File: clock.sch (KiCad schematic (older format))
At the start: 20 parts, among them SW1 SW_Push, SW2 SW_SPDT, U23 LM555xN, U24 74LS04, U25 74LS08, U26 74LS32, U27 LM555xN, U28 LM555xN

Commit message: Let there be light
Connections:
- no-connect marks 3 -> 2
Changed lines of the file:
@@
 $Descr A4 11693 8268
 encoding utf-8
-Sheet 5 11
+Sheet 8 20
 Title ""
 Date ""
@@
 	1    0    0    -1
 $EndComp
-NoConn ~ 5450 5050
 $EndSCHEMATC

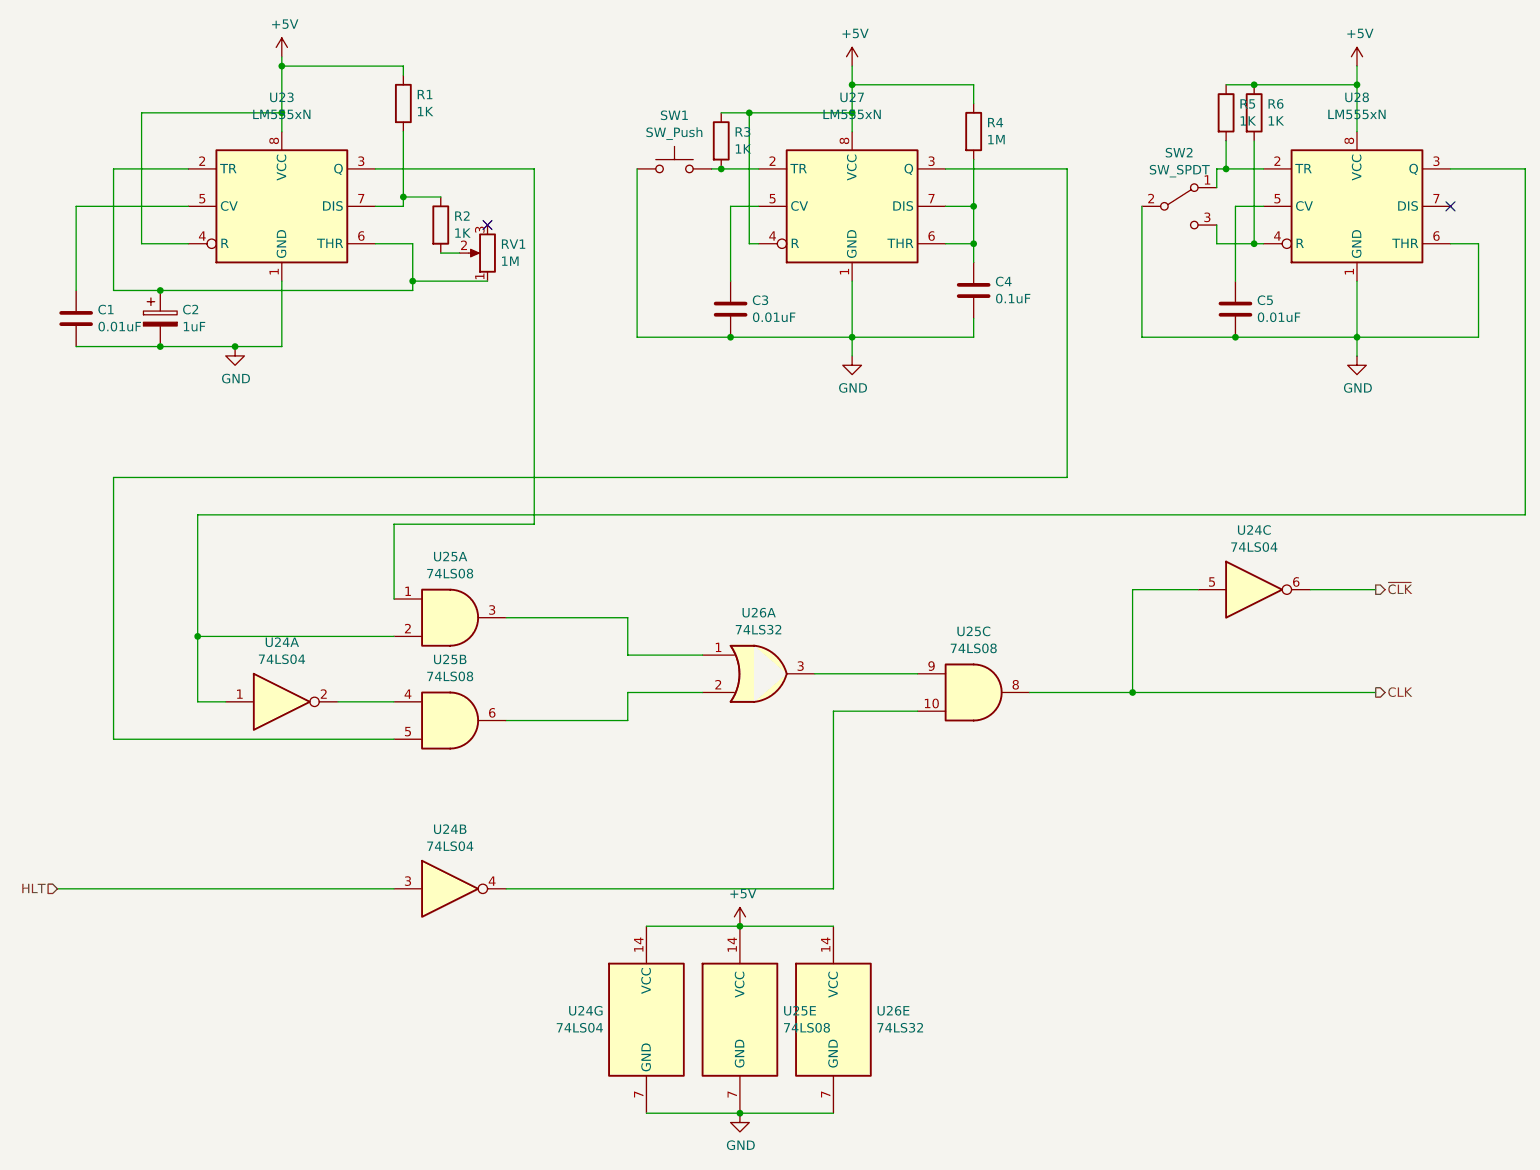
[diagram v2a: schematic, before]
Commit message: Added NAND GATES in ALU
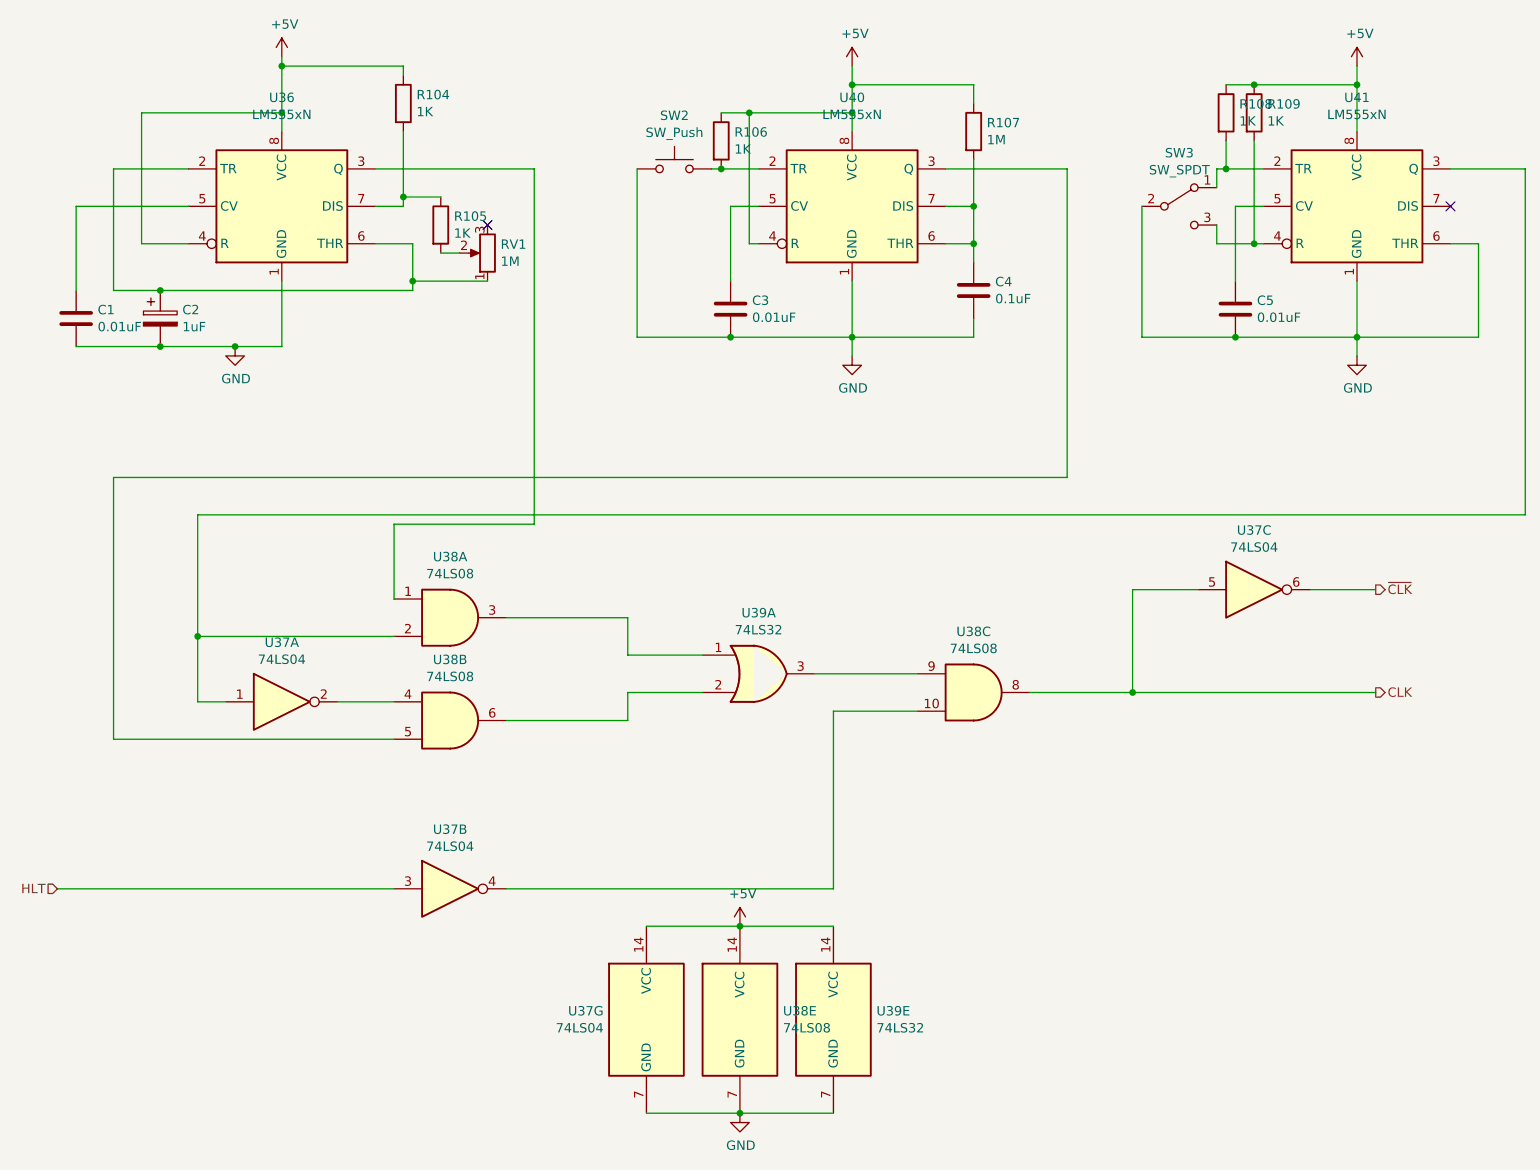
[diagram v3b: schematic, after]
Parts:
- renumbered R1 to R104, R2 to R105, R3 to R106, R4 to R107, R5 to R108, R6 to R109, SW1 to SW2, SW2 to SW3, U23 to U36, U24 to U37, U25 to U38, U26 to U39, U27 to U40, U28 to U41

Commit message: using new RAM and ROM,15bits baby
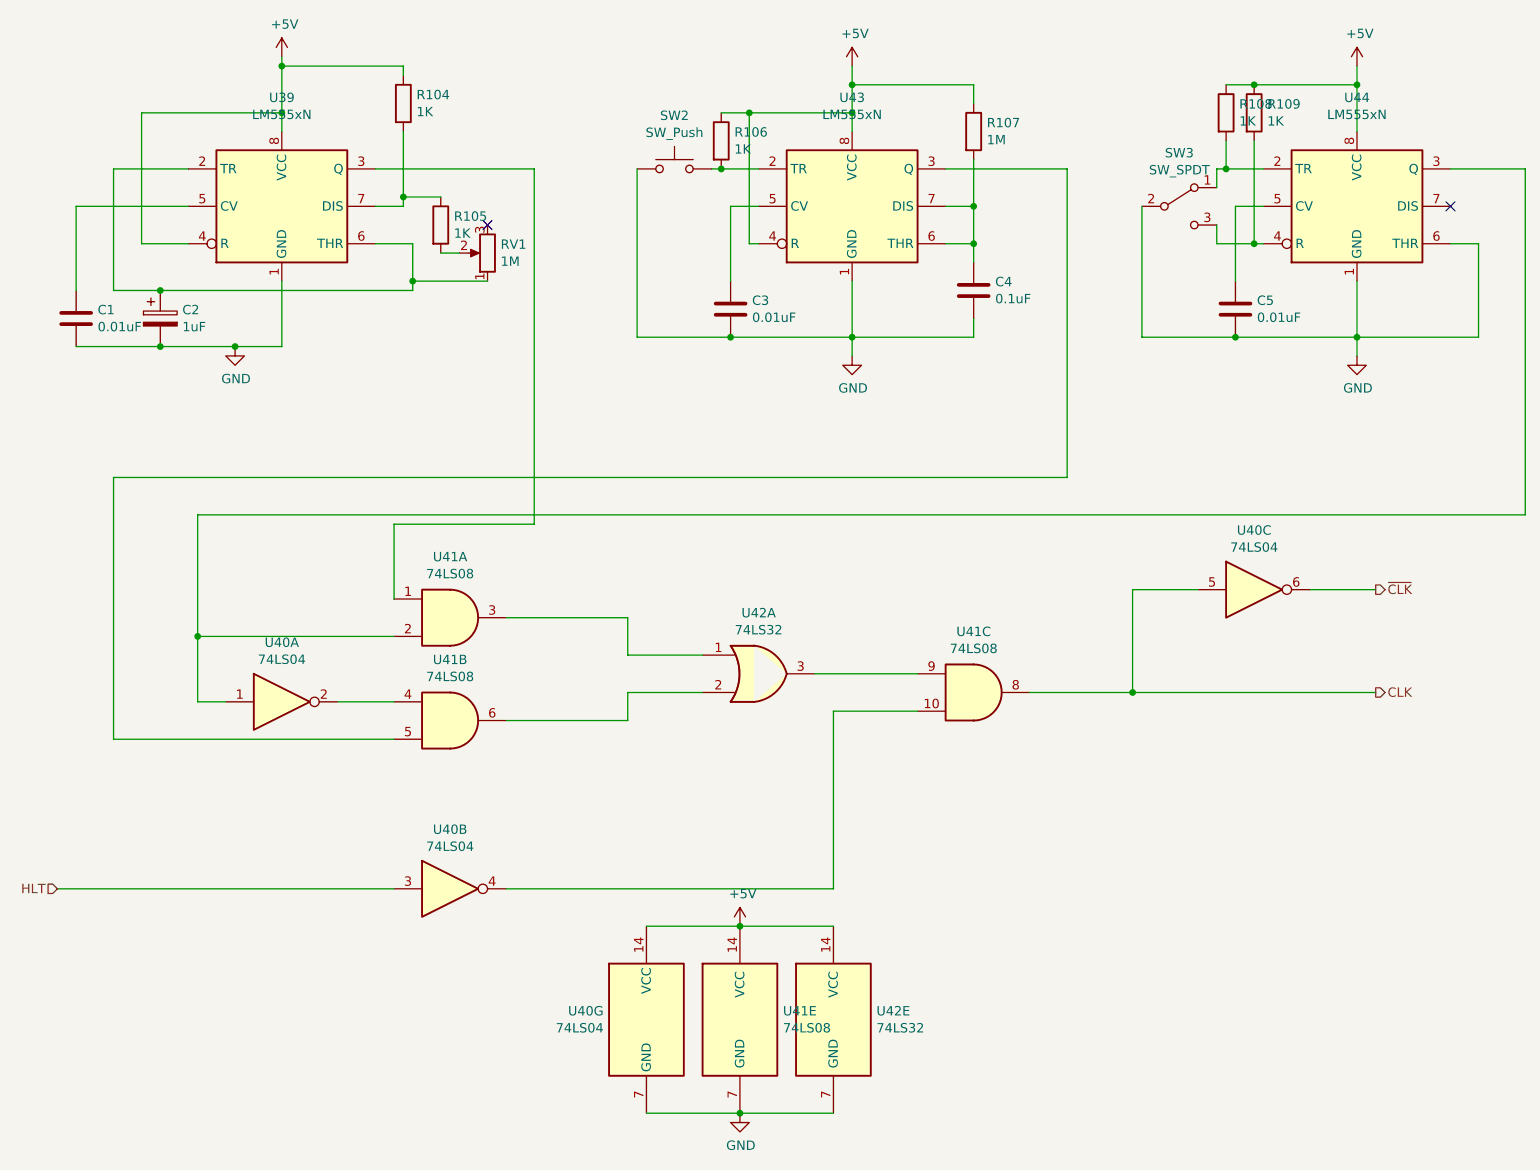
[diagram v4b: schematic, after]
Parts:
- renumbered U36 to U39, U37 to U40, U38 to U41, U39 to U42, U40 to U43, U41 to U44
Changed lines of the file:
@@
 P 2700 1100
 AR Path="/5F76260D" Ref="#PWR?"  Part="1"
-AR Path="/5F75E433/5F76260D" Ref="#PWR0151"  Part="1"
-F 0 "#PWR0151" H 2700 950 50  0001 C CNN
+AR Path="/5F75E433/5F76260D" Ref="#PWR0156"  Part="1"
+F 0 "#PWR0156" H 2700 950 50  0001 C CNN
 F 1 "+5V" H 2715 1273 50  0000 C CNN
 F 2 "" H 2700 1100 50  0001 C CNN
@@
 P 5750 2700
 AR Path="/5F763381" Ref="#PWR?"  Part="1"
-AR Path="/5F75E433/5F763381" Ref="#PWR0155"  Part="1"
-F 0 "#PWR0155" H 5750 2450 50  0001 C CNN
+AR Path="/5F75E433/5F763381" Ref="#PWR0160"  Part="1"
+F 0 "#PWR0160" H 5750 2450 50  0001 C CNN
 F 1 "GND" H 5755 2527 50  0000 C CNN
 F 2 "" H 5750 2700 50  0001 C CNN
@@
 P 2450 2650
 AR Path="/5F7634B3" Ref="#PWR?"  Part="1"
-AR Path="/5F75E433/5F7634B3" Ref="#PWR0150"  Part="1"
-F 0 "#PWR0150" H 2450 2400 50  0001 C CNN
+AR Path="/5F75E433/5F7634B3" Ref="#PWR0155"  Part="1"
+F 0 "#PWR0155" H 2450 2400 50  0001 C CNN
 F 1 "GND" H 2455 2477 50  0000 C CNN
 F 2 "" H 2450 2650 50  0001 C CNN
@@
 P 5750 1150
 AR Path="/5F76F8D8" Ref="#PWR?"  Part="1"
-AR Path="/5F75E433/5F76F8D8" Ref="#PWR0154"  Part="1"
-F 0 "#PWR0154" H 5750 1000 50  0001 C CNN
+AR Path="/5F75E433/5F76F8D8" Ref="#PWR0159"  Part="1"
+F 0 "#PWR0159" H 5750 1000 50  0001 C CNN
 F 1 "+5V" H 5765 1323 50  0000 C CNN
 F 2 "" H 5750 1150 50  0001 C CNN
@@
 P 8450 2700
 AR Path="/5F785279" Ref="#PWR?"  Part="1"
-AR Path="/5F75E433/5F785279" Ref="#PWR0157"  Part="1"
-F 0 "#PWR0157" H 8450 2450 50  0001 C CNN
+AR Path="/5F75E433/5F785279" Ref="#PWR0162"  Part="1"
+F 0 "#PWR0162" H 8450 2450 50  0001 C CNN
 F 1 "GND" H 8455 2527 50  0000 C CNN
 F 2 "" H 8450 2700 50  0001 C CNN
@@
 P 8450 1150
 AR Path="/5F78527F" Ref="#PWR?"  Part="1"
-AR Path="/5F75E433/5F78527F" Ref="#PWR0156"  Part="1"
-F 0 "#PWR0156" H 8450 1000 50  0001 C CNN
+AR Path="/5F75E433/5F78527F" Ref="#PWR0161"  Part="1"
+F 0 "#PWR0161" H 8450 1000 50  0001 C CNN
 F 1 "+5V" H 8465 1323 50  0000 C CNN
 F 2 "" H 8450 1150 50  0001 C CNN
@@
 P 3600 4100
 AR Path="/5F7BE3EA" Ref="U?"  Part="1"
-AR Path="/5F75E433/5F7BE3EA" Ref="U38"  Part="1"
-F 0 "U38" H 3600 4425 50  0000 C CNN
+AR Path="/5F75E433/5F7BE3EA" Ref="U41"  Part="1"
+F 0 "U41" H 3600 4425 50  0000 C CNN
 F 1 "74LS08" H 3600 4334 50  0000 C CNN
 F 2 "Package_DIP:DIP-14_W7.62mm" H 3600 4100 50  0001 C CNN
@@
 P 3600 4650
 AR Path="/5F7C112B" Ref="U?"  Part="2"
-AR Path="/5F75E433/5F7C112B" Ref="U38"  Part="2"
-F 0 "U38" H 3600 4975 50  0000 C CNN
+AR Path="/5F75E433/5F7C112B" Ref="U41"  Part="2"
+F 0 "U41" H 3600 4975 50  0000 C CNN
 F 1 "74LS08" H 3600 4884 50  0000 C CNN
 F 2 "Package_DIP:DIP-14_W7.62mm" H 3600 4650 50  0001 C CNN
@@
 P 6400 4500
 AR Path="/5F7C255C" Ref="U?"  Part="3"
-AR Path="/5F75E433/5F7C255C" Ref="U38"  Part="3"
-F 0 "U38" H 6400 4825 50  0000 C CNN
+AR Path="/5F75E433/5F7C255C" Ref="U41"  Part="3"
+F 0 "U41" H 6400 4825 50  0000 C CNN
 F 1 "74LS08" H 6400 4734 50  0000 C CNN
 F 2 "Package_DIP:DIP-14_W7.62mm" H 6400 4500 50  0001 C CNN
@@
 P 5250 4400
 AR Path="/5F7C6F12" Ref="U?"  Part="1"
-AR Path="/5F75E433/5F7C6F12" Ref="U39"  Part="1"
-F 0 "U39" H 5250 4725 50  0000 C CNN
+AR Path="/5F75E433/5F7C6F12" Ref="U42"  Part="1"
+F 0 "U42" H 5250 4725 50  0000 C CNN
 F 1 "74LS32" H 5250 4634 50  0000 C CNN
 F 2 "Package_DIP:DIP-14_W7.62mm" H 5250 4400 50  0001 C CNN
@@
 P 2700 4550
 AR Path="/5F7CE7FD" Ref="U?"  Part="1"
-AR Path="/5F75E433/5F7CE7FD" Ref="U37"  Part="1"
-F 0 "U37" H 2700 4867 50  0000 C CNN
+AR Path="/5F75E433/5F7CE7FD" Ref="U40"  Part="1"
+F 0 "U40" H 2700 4867 50  0000 C CNN
 F 1 "74LS04" H 2700 4776 50  0000 C CNN
 F 2 "Package_DIP:DIP-14_W7.62mm" H 2700 4550 50  0001 C CNN
@@
 P 3600 5550
 AR Path="/5F7D01D9" Ref="U?"  Part="2"
-AR Path="/5F75E433/5F7D01D9" Ref="U37"  Part="2"
-F 0 "U37" H 3600 5867 50  0000 C CNN
+AR Path="/5F75E433/5F7D01D9" Ref="U40"  Part="2"
+F 0 "U40" H 3600 5867 50  0000 C CNN
 F 1 "74LS04" H 3600 5776 50  0000 C CNN
 F 2 "Package_DIP:DIP-14_W7.62mm" H 3600 5550 50  0001 C CNN
@@
 P 7900 3950
 AR Path="/5F7D1AFC" Ref="U?"  Part="3"
-AR Path="/5F75E433/5F7D1AFC" Ref="U37"  Part="3"
-F 0 "U37" H 7900 4267 50  0000 C CNN
+AR Path="/5F75E433/5F7D1AFC" Ref="U40"  Part="3"
+F 0 "U40" H 7900 4267 50  0000 C CNN
 F 1 "74LS04" H 7900 4176 50  0000 C CNN
 F 2 "Package_DIP:DIP-14_W7.62mm" H 7900 3950 50  0001 C CNN
@@
 P 5150 5750
 AR Path="/6081D7D4" Ref="#PWR?"  Part="1"
-AR Path="/5F75E433/6081D7D4" Ref="#PWR0152"  Part="1"
-F 0 "#PWR0152" H 5150 5600 50  0001 C CNN
+AR Path="/5F75E433/6081D7D4" Ref="#PWR0157"  Part="1"
+F 0 "#PWR0157" H 5150 5600 50  0001 C CNN
 F 1 "+5V" H 5165 5923 50  0000 C CNN
 F 2 "" H 5150 5750 50  0001 C CNN
@@
 P 5150 6750
 AR Path="/6081E349" Ref="#PWR?"  Part="1"
-AR Path="/5F75E433/6081E349" Ref="#PWR0153"  Part="1"
-F 0 "#PWR0153" H 5150 6500 50  0001 C CNN
+AR Path="/5F75E433/6081E349" Ref="#PWR0158"  Part="1"
+F 0 "#PWR0158" H 5150 6500 50  0001 C CNN
 F 1 "GND" H 5155 6577 50  0000 C CNN
 F 2 "" H 5150 6750 50  0001 C CNN
@@
 P 4650 6250
 AR Path="/6085491F" Ref="U?"  Part="7"
-AR Path="/5F75E433/6085491F" Ref="U37"  Part="7"
-F 0 "U37" H 4421 6296 50  0000 R CNN
+AR Path="/5F75E433/6085491F" Ref="U40"  Part="7"
+F 0 "U40" H 4421 6296 50  0000 R CNN
 F 1 "74LS04" H 4421 6205 50  0000 R CNN
 F 2 "Package_DIP:DIP-14_W7.62mm" H 4650 6250 50  0001 C CNN
@@
 P 5150 6250
 AR Path="/6085870D" Ref="U?"  Part="5"
-AR Path="/5F75E433/6085870D" Ref="U38"  Part="5"
-F 0 "U38" H 5380 6296 50  0000 L CNN
+AR Path="/5F75E433/6085870D" Ref="U41"  Part="5"
+F 0 "U41" H 5380 6296 50  0000 L CNN
 F 1 "74LS08" H 5380 6205 50  0000 L CNN
 F 2 "Package_DIP:DIP-14_W7.62mm" H 5150 6250 50  0001 C CNN
@@
 P 5650 6250
 AR Path="/608654F6" Ref="U?"  Part="5"
-AR Path="/5F75E433/608654F6" Ref="U39"  Part="5"
-F 0 "U39" H 5880 6296 50  0000 L CNN
+AR Path="/5F75E433/608654F6" Ref="U42"  Part="5"
+F 0 "U42" H 5880 6296 50  0000 L CNN
 F 1 "74LS32" H 5880 6205 50  0000 L CNN
 F 2 "Package_DIP:DIP-14_W7.62mm" H 5650 6250 50  0001 C CNN
@@
 P 2700 1900
 AR Path="/60AA52FF" Ref="U?"  Part="1"
-AR Path="/5F75E433/60AA52FF" Ref="U36"  Part="1"
-F 0 "U36" H 2700 2481 50  0000 C CNN
+AR Path="/5F75E433/60AA52FF" Ref="U39"  Part="1"
+F 0 "U39" H 2700 2481 50  0000 C CNN
 F 1 "LM555xN" H 2700 2390 50  0000 C CNN
 F 2 "Package_DIP:DIP-8_W7.62mm" H 3350 1500 50  0001 C CNN
@@
 P 5750 1900
 AR Path="/60AB8137" Ref="U?"  Part="1"
-AR Path="/5F75E433/60AB8137" Ref="U40"  Part="1"
-F 0 "U40" H 5750 2481 50  0000 C CNN
+AR Path="/5F75E433/60AB8137" Ref="U43"  Part="1"
+F 0 "U43" H 5750 2481 50  0000 C CNN
 F 1 "LM555xN" H 5750 2390 50  0000 C CNN
 F 2 "Package_DIP:DIP-8_W7.62mm" H 6400 1500 50  0001 C CNN
@@
 P 8450 1900
 AR Path="/60AB9E78" Ref="U?"  Part="1"
-AR Path="/5F75E433/60AB9E78" Ref="U41"  Part="1"
-F 0 "U41" H 8450 2481 50  0000 C CNN
+AR Path="/5F75E433/60AB9E78" Ref="U44"  Part="1"
+F 0 "U44" H 8450 2481 50  0000 C CNN
 F 1 "LM555xN" H 8450 2390 50  0000 C CNN
 F 2 "Package_DIP:DIP-8_W7.62mm" H 9100 1500 50  0001 C CNN

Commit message: using new ROM in CU and more jumps
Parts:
- renumbered U39 to U38, U40 to U39, U41 to U40, U42 to U41, U43 to U42, U44 to U43
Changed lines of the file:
@@
 P 3600 4100
 AR Path="/5F7BE3EA" Ref="U?"  Part="1"
-AR Path="/5F75E433/5F7BE3EA" Ref="U41"  Part="1"
-F 0 "U41" H 3600 4425 50  0000 C CNN
+AR Path="/5F75E433/5F7BE3EA" Ref="U40"  Part="1"
+F 0 "U40" H 3600 4425 50  0000 C CNN
 F 1 "74LS08" H 3600 4334 50  0000 C CNN
 F 2 "Package_DIP:DIP-14_W7.62mm" H 3600 4100 50  0001 C CNN
@@
 P 3600 4650
 AR Path="/5F7C112B" Ref="U?"  Part="2"
-AR Path="/5F75E433/5F7C112B" Ref="U41"  Part="2"
-F 0 "U41" H 3600 4975 50  0000 C CNN
+AR Path="/5F75E433/5F7C112B" Ref="U40"  Part="2"
+F 0 "U40" H 3600 4975 50  0000 C CNN
 F 1 "74LS08" H 3600 4884 50  0000 C CNN
 F 2 "Package_DIP:DIP-14_W7.62mm" H 3600 4650 50  0001 C CNN
@@
 P 6400 4500
 AR Path="/5F7C255C" Ref="U?"  Part="3"
-AR Path="/5F75E433/5F7C255C" Ref="U41"  Part="3"
-F 0 "U41" H 6400 4825 50  0000 C CNN
+AR Path="/5F75E433/5F7C255C" Ref="U40"  Part="3"
+F 0 "U40" H 6400 4825 50  0000 C CNN
 F 1 "74LS08" H 6400 4734 50  0000 C CNN
 F 2 "Package_DIP:DIP-14_W7.62mm" H 6400 4500 50  0001 C CNN
@@
 P 5250 4400
 AR Path="/5F7C6F12" Ref="U?"  Part="1"
-AR Path="/5F75E433/5F7C6F12" Ref="U42"  Part="1"
-F 0 "U42" H 5250 4725 50  0000 C CNN
+AR Path="/5F75E433/5F7C6F12" Ref="U41"  Part="1"
+F 0 "U41" H 5250 4725 50  0000 C CNN
 F 1 "74LS32" H 5250 4634 50  0000 C CNN
 F 2 "Package_DIP:DIP-14_W7.62mm" H 5250 4400 50  0001 C CNN
@@
 P 2700 4550
 AR Path="/5F7CE7FD" Ref="U?"  Part="1"
-AR Path="/5F75E433/5F7CE7FD" Ref="U40"  Part="1"
-F 0 "U40" H 2700 4867 50  0000 C CNN
+AR Path="/5F75E433/5F7CE7FD" Ref="U39"  Part="1"
+F 0 "U39" H 2700 4867 50  0000 C CNN
 F 1 "74LS04" H 2700 4776 50  0000 C CNN
 F 2 "Package_DIP:DIP-14_W7.62mm" H 2700 4550 50  0001 C CNN
@@
 P 3600 5550
 AR Path="/5F7D01D9" Ref="U?"  Part="2"
-AR Path="/5F75E433/5F7D01D9" Ref="U40"  Part="2"
-F 0 "U40" H 3600 5867 50  0000 C CNN
+AR Path="/5F75E433/5F7D01D9" Ref="U39"  Part="2"
+F 0 "U39" H 3600 5867 50  0000 C CNN
 F 1 "74LS04" H 3600 5776 50  0000 C CNN
 F 2 "Package_DIP:DIP-14_W7.62mm" H 3600 5550 50  0001 C CNN
@@
 P 7900 3950
 AR Path="/5F7D1AFC" Ref="U?"  Part="3"
-AR Path="/5F75E433/5F7D1AFC" Ref="U40"  Part="3"
-F 0 "U40" H 7900 4267 50  0000 C CNN
+AR Path="/5F75E433/5F7D1AFC" Ref="U39"  Part="3"
+F 0 "U39" H 7900 4267 50  0000 C CNN
 F 1 "74LS04" H 7900 4176 50  0000 C CNN
 F 2 "Package_DIP:DIP-14_W7.62mm" H 7900 3950 50  0001 C CNN
@@
 P 4650 6250
 AR Path="/6085491F" Ref="U?"  Part="7"
-AR Path="/5F75E433/6085491F" Ref="U40"  Part="7"
-F 0 "U40" H 4421 6296 50  0000 R CNN
+AR Path="/5F75E433/6085491F" Ref="U39"  Part="7"
+F 0 "U39" H 4421 6296 50  0000 R CNN
 F 1 "74LS04" H 4421 6205 50  0000 R CNN
 F 2 "Package_DIP:DIP-14_W7.62mm" H 4650 6250 50  0001 C CNN
@@
 P 5150 6250
 AR Path="/6085870D" Ref="U?"  Part="5"
-AR Path="/5F75E433/6085870D" Ref="U41"  Part="5"
-F 0 "U41" H 5380 6296 50  0000 L CNN
+AR Path="/5F75E433/6085870D" Ref="U40"  Part="5"
+F 0 "U40" H 5380 6296 50  0000 L CNN
 F 1 "74LS08" H 5380 6205 50  0000 L CNN
 F 2 "Package_DIP:DIP-14_W7.62mm" H 5150 6250 50  0001 C CNN
@@
 P 5650 6250
 AR Path="/608654F6" Ref="U?"  Part="5"
-AR Path="/5F75E433/608654F6" Ref="U42"  Part="5"
-F 0 "U42" H 5880 6296 50  0000 L CNN
+AR Path="/5F75E433/608654F6" Ref="U41"  Part="5"
+F 0 "U41" H 5880 6296 50  0000 L CNN
 F 1 "74LS32" H 5880 6205 50  0000 L CNN
 F 2 "Package_DIP:DIP-14_W7.62mm" H 5650 6250 50  0001 C CNN
@@
 P 2700 1900
 AR Path="/60AA52FF" Ref="U?"  Part="1"
-AR Path="/5F75E433/60AA52FF" Ref="U39"  Part="1"
-F 0 "U39" H 2700 2481 50  0000 C CNN
+AR Path="/5F75E433/60AA52FF" Ref="U38"  Part="1"
+F 0 "U38" H 2700 2481 50  0000 C CNN
 F 1 "LM555xN" H 2700 2390 50  0000 C CNN
 F 2 "Package_DIP:DIP-8_W7.62mm" H 3350 1500 50  0001 C CNN
@@
 P 5750 1900
 AR Path="/60AB8137" Ref="U?"  Part="1"
-AR Path="/5F75E433/60AB8137" Ref="U43"  Part="1"
-F 0 "U43" H 5750 2481 50  0000 C CNN
+AR Path="/5F75E433/60AB8137" Ref="U42"  Part="1"
+F 0 "U42" H 5750 2481 50  0000 C CNN
 F 1 "LM555xN" H 5750 2390 50  0000 C CNN
 F 2 "Package_DIP:DIP-8_W7.62mm" H 6400 1500 50  0001 C CNN
@@
 P 8450 1900
 AR Path="/60AB9E78" Ref="U?"  Part="1"
-AR Path="/5F75E433/60AB9E78" Ref="U44"  Part="1"
-F 0 "U44" H 8450 2481 50  0000 C CNN
+AR Path="/5F75E433/60AB9E78" Ref="U43"  Part="1"
+F 0 "U43" H 8450 2481 50  0000 C CNN
 F 1 "LM555xN" H 8450 2390 50  0000 C CNN
 F 2 "Package_DIP:DIP-8_W7.62mm" H 9100 1500 50  0001 C CNN
